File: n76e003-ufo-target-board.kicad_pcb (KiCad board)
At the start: 2 copper layers, 52.3 x 68.1 mm, 11 parts, among them J1 CW308T_CONNBOARD, U2 N76E003AT20

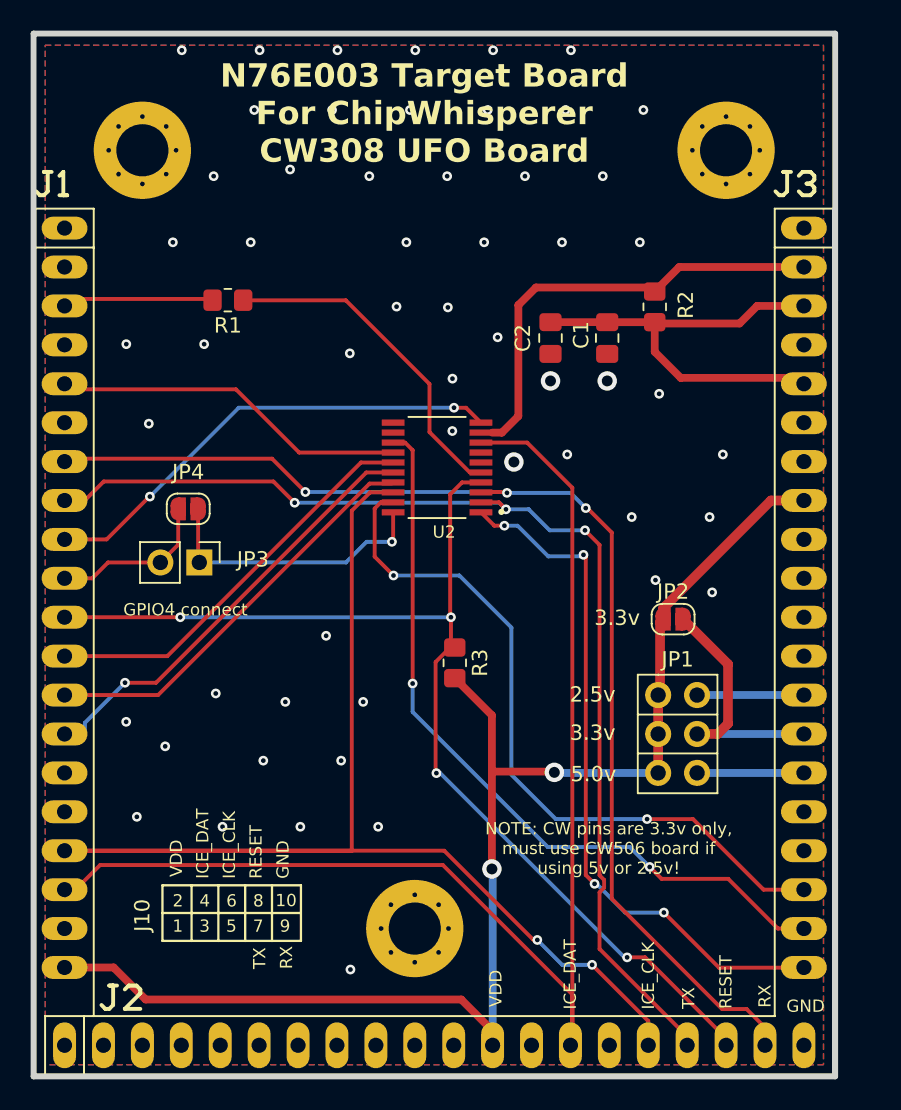
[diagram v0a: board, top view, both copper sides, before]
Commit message: Remove C2, add url to board
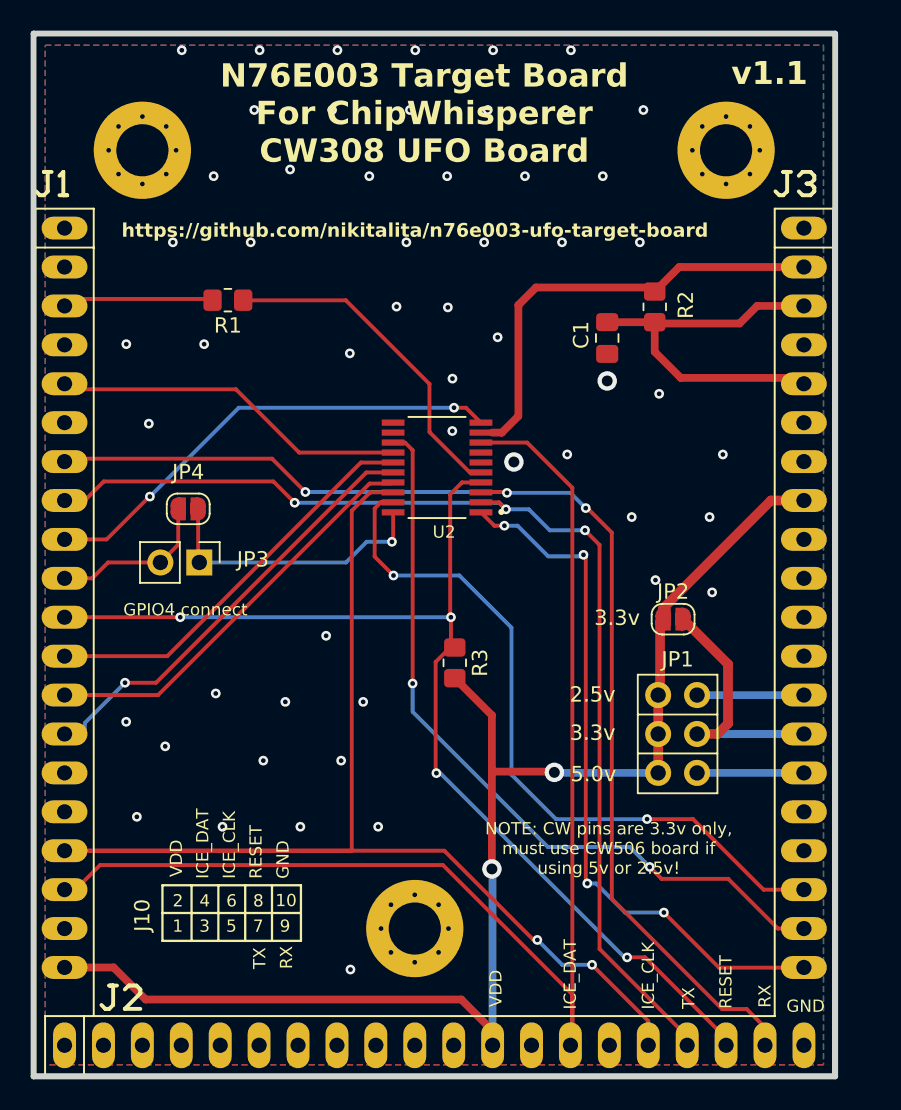
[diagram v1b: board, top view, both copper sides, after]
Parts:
- removed C2: 2.2uF, Capacitor_SMD:C_0805_2012Metric_Pad1.18x1.45mm_HandSolder
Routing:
- net Net-(J1-FILT_LP): track 28.9 -> 25.2 mm
- net GND: vias 56 -> 55
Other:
- board text added: "https://github.com/nikitalita/n76e003-ufo-target-board"
- board text added: "v1.1"
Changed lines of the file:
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@@
-  )
-  (footprint "Capacitor_SMD:C_0805_2012Metric_Pad1.18x1.45mm_HandSolder" (layer "F.Cu")
-    (at 156.3 83 -90)
-    (descr "Capacitor SMD 0805 (2012 Metric), square (rectangular) end terminal, IPC_7351 nominal with elongated pad for handsoldering. (Body size source: IPC-SM-782 page 76, https://www.pcb-3d.com/wordpress/wp-content/uploads/ipc-sm-782a_amendment_1_and_2.pdf, https://docs.google.com/spreadsheets/d/1BsfQQcO9C6DZCsRaXUlFlo91Tg2WpOkGARC1WS5S8t0/edit?usp=sharing), generated with kicad-footprint-generator")
-    (tags "capacitor handsolder")
-    (property "Sheetfile" "n76e003-ufo-target-board.kicad_sch")
-    (property "Sheetname" "")
-    (property "ki_description" "Unpolarized capacitor, small symbol")
-    (property "ki_keywords" "capacitor cap")
-    (attr smd)
-    (fp_text reference "C2" (at 0 1.8 -90) (layer "F.SilkS")
-        (effects (font (size 1 1) (thickness 0.15)))
-    )
-    (fp_text value "2.2uF" (at 0 1.68 -90) (layer "F.Fab")
-        (effects (font (size 1 1) (thickness 0.15)))
-    )
-    (fp_text user "${REFERENCE}" (at 0 0 -90) (layer "F.Fab")
-        (effects (font (size 0.5 0.5) (thickness 0.08)))
-    )
-    (fp_line (start -0.261252 -0.735) (end 0.261252 -0.735)
-      (stroke (width 0.12) (type solid)) (layer "F.SilkS"))
-    (fp_line (start -0.261252 0.735) (end 0.261252 0.735)
-      (stroke (width 0.12) (type solid)) (layer "F.SilkS"))
-    (fp_line (start -1.88 -0.98) (end 1.88 -0.98)
-      (stroke (width 0.05) (type solid)) (layer "F.CrtYd"))
-    (fp_line (start -1.88 0.98) (end -1.88 -0.98)
-      (stroke (width 0.05) (type solid)) (layer "F.CrtYd"))
-    (fp_line (start 1.88 -0.98) (end 1.88 0.98)
-      (stroke (width 0.05) (type solid)) (layer "F.CrtYd"))
-    (fp_line (start 1.88 0.98) (end -1.88 0.98)
-      (stroke (width 0.05) (type solid)) (layer "F.CrtYd"))
-    (fp_line (start -1 -0.625) (end 1 -0.625)
-      (stroke (width 0.1) (type solid)) (layer "F.Fab"))
-    (fp_line (start -1 0.625) (end -1 -0.625)
-      (stroke (width 0.1) (type solid)) (layer "F.Fab"))
-    (fp_line (start 1 -0.625) (end 1 0.625)
-      (stroke (width 0.1) (type solid)) (layer "F.Fab"))
-    (fp_line (start 1 0.625) (end -1 0.625)
-      (stroke (width 0.1) (type solid)) (layer "F.Fab"))
-    (pad "1" smd roundrect (at -1.0375 0 270) (size 1.175 1.45) (layers "F.Cu" "F.Paste" "F.Mask") (roundrect_rratio 0.2127659574)
-      (net 3 "Net-(J1-FILT_LP)") (pintype "passive"))
-    (pad "2" smd roundrect (at 1.0375 0 270) (size 1.175 1.45) (layers "F.Cu" "F.Paste" "F.Mask") (roundrect_rratio 0.2127659574)
-      (net 2 "GND") (pintype "passive"))
-    (model "${KICAD6_3DMODEL_DIR}/Capacitor_SMD.3dshapes/C_0805_2012Metric.wrl"
-      (offset (xyz 0 0 0))
-      (scale (xyz 1 1 1))
-      (rotate (xyz 0 0 0))
-    )
   )
   (footprint "Capacitor_SMD:C_0805_2012Metric_Pad1.18x1.45mm_HandSolder" (layer "F.Cu")
@@
     (effects (font (size 1.524 1.524) (thickness 0.254) bold) (justify bottom))
   )
+  (gr_text "https://github.com/nikitalita/n76e003-ufo-target-board" (at 128.3 76.5) (layer "F.SilkS")
+    (effects (font (size 0.9 0.9) (thickness 0.2) bold) (justify left bottom))
+  )
   (gr_text "2" (at 131.63 120.2) (layer "F.SilkS")
     (effects (font (size 0.8 0.8) (thickness 0.15)) (justify left bottom))
@@
   (gr_text "6" (at 135.13 120.2) (layer "F.SilkS")
     (effects (font (size 0.8 0.8) (thickness 0.15)) (justify left bottom))
+  )
+  (gr_text "v1.1" (at 168.1 66.6) (layer "F.SilkS")
+    (effects (font (size 1.5 1.5) (thickness 0.3) bold) (justify left bottom))
   )
   (gr_text "RX" (at 170.760212 126.713363 90) (layer "F.SilkS")
@@
   (via (at 154.632 72.435) (size 0.635) (drill 0.3048) (layers "F.Cu" "B.Cu") (net 2))
   (via (at 149.6 81) (size 0.635) (drill 0.3048) (layers "F.Cu" "B.Cu") (free) (net 2))
-  (via (at 156.3 85.8) (size 1.27) (drill 0.7112) (layers "F.Cu" "B.Cu") (free) (net 2))
   (via (at 163.15 98.8) (size 0.635) (drill 0.3048) (layers "F.Cu" "B.Cu") (net 2))
   (via (at 149.89 89.07) (size 0.635) (drill 0.3048) (layers "F.Cu" "B.Cu") (free) (net 2))
@@
   (via (at 143.2 84) (size 0.635) (drill 0.3048) (layers "F.Cu" "B.Cu") (net 2))
   (segment (start 164.8 85.6) (end 172.4553 85.6) (width 0.508) (layer "F.Cu") (net 3))
-  (segment (start 156.3 81.9625) (end 159.995 81.9625) (width 0.508) (layer "F.Cu") (net 3))
   (segment (start 169.7858 80.9042) (end 168.64 82.05) (width 0.508) (layer "F.Cu") (net 3))
   (segment (start 163.1025 81.965) (end 163.1025 83.9025) (width 0.508) (layer "F.Cu") (net 3))
@@
   (segment (start 158.6 94.1) (end 157.606537 93.106537) (width 0.254) (layer "B.Cu") (net 6))
   (segment (start 152.935 93.725) (end 151.7575 93.725) (width 0.254) (layer "F.Cu") (net 7))
-  (segment (start 159.7973 118.367234) (end 159.7973 118.882766) (width 0.254) (layer "F.Cu") (net 7))
-  (segment (start 159.5 118.069934) (end 159.7973 118.367234) (width 0.254) (layer "F.Cu") (net 7))
+  (segment (start 158.55 95.55) (end 159.5 96.5) (width 0.254) (layer "F.Cu") (net 7))
   (segment (start 127.1373 92.3627) (end 125.8958 93.6042) (width 0.254) (layer "F.Cu") (net 7))
-  (segment (start 158.55 95.55) (end 159.5 96.5) (width 0.254) (layer "F.Cu") (net 7))
   (segment (start 159.5 122.875) (end 165.2195 128.5945) (width 0.254) (layer "F.Cu") (net 7))
+  (segment (start 159.5 96.5) (end 159.5 122.875) (width 0.254) (layer "F.Cu") (net 7))
   (segment (start 125.8958 93.6042) (end 124.5795 93.6042) (width 0.254) (layer "F.Cu") (net 7))
   (segment (start 138.2127 92.3627) (end 127.1373 92.3627) (width 0.254) (layer "F.Cu") (net 7))
-  (segment (start 159.7973 118.882766) (end 159.5 119.180066) (width 0.254) (layer "F.Cu") (net 7))
-  (segment (start 159.5 119.180066) (end 159.5 122.875) (width 0.254) (layer "F.Cu") (net 7))
-  (segment (start 159.5 96.5) (end 159.5 118.069934) (width 0.254) (layer "F.Cu") (net 7))
   (segment (start 153.39 94.18) (end 152.935 93.725) (width 0.254) (layer "F.Cu") (net 7))
   (segment (start 139.6 93.75) (end 138.2127 92.3627) (width 0.254) (layer "F.Cu") (net 7))
@@
   (segment (start 147.3 105.55) (end 147.3 107.4) (width 0.254) (layer "B.Cu") (net 34))
   (segment (start 156.125 116.225) (end 161.475 116.225) (width 0.254) (layer "B.Cu") (net 34))
-  (segment (start 159.175 118.625) (end 158.6 118.05) (width 0.254) (layer "F.Cu") (net 35))
+  (segment (start 158.7 118.6) (end 158.6 118.5) (width 0.254) (layer "F.Cu") (net 35))
+  (segment (start 158.6 118.5) (end 158.6 97.3) (width 0.254) (layer "F.Cu") (net 35))
+  (segment (start 152.6325 95.25) (end 151.7575 94.375) (width 0.254) (layer "F.Cu") (net 35))
   (segment (start 158.6 97.3) (end 158.45 97.15) (width 0.254) (layer "F.Cu") (net 35))
-  (segment (start 152.6325 95.25) (end 151.7575 94.375) (width 0.254) (layer "F.Cu") (net 35))
-  (segment (start 158.6 118.05) (end 158.6 97.3) (width 0.254) (layer "F.Cu") (net 35))
   (segment (start 167.3 124.1) (end 172.8237 124.1) (width 0.254) (layer "F.Cu") (net 35))
   (segment (start 153.29 95.25) (end 152.6325 95.25) (width 0.254) (layer "F.Cu") (net 35))
@@
   (via (at 153.29 95.25) (size 0.635) (drill 0.3048) (layers "F.Cu" "B.Cu") (net 35))
   (via (at 163.7 120.5) (size 0.635) (drill 0.3048) (layers "F.Cu" "B.Cu") (net 35))
-  (via (at 159.175 118.625) (size 0.635) (drill 0.3048) (layers "F.Cu" "B.Cu") (net 35))
-  (segment (start 161.175 120.5) (end 159.3 118.625) (width 0.254) (layer "B.Cu") (net 35))
-  (segment (start 163.7 120.5) (end 161.175 120.5) (width 0.254) (layer "B.Cu") (net 35))
-  (segment (start 159.3 118.625) (end 159.175 118.625) (width 0.254) (layer "B.Cu") (net 35))
+  (via (at 158.7 118.6) (size 0.635) (drill 0.3048) (layers "F.Cu" "B.Cu") (net 35))
   (segment (start 154.15 95.25) (end 156.15 97.25) (width 0.254) (layer "B.Cu") (net 35))
+  (segment (start 158.7 118.6) (end 159.275 118.6) (width 0.254) (layer "B.Cu") (net 35))
   (segment (start 158.35 97.25) (end 158.45 97.15) (width 0.254) (layer "B.Cu") (net 35))
+  (segment (start 161.175 120.5) (end 163.7 120.5) (width 0.254) (layer "B.Cu") (net 35))
   (segment (start 153.29 95.25) (end 154.15 95.25) (width 0.254) (layer "B.Cu") (net 35))
+  (segment (start 159.275 118.6) (end 161.175 120.5) (width 0.254) (layer "B.Cu") (net 35))
   (segment (start 156.15 97.25) (end 158.35 97.25) (width 0.254) (layer "B.Cu") (net 35))
   (segment (start 125.0137 86.35) (end 135.77 86.35) (width 0.254) (layer "F.Cu") (net 36))
